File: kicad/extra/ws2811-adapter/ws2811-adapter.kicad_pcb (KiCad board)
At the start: 2 copper layers, 70 x 30 mm, 12 parts, among them J1 Conn_01x03_Pin, J2 RJ45 P1, J3 RJ45 P2, J4 RJ45 P3, J5 Conn_01x03_Socket

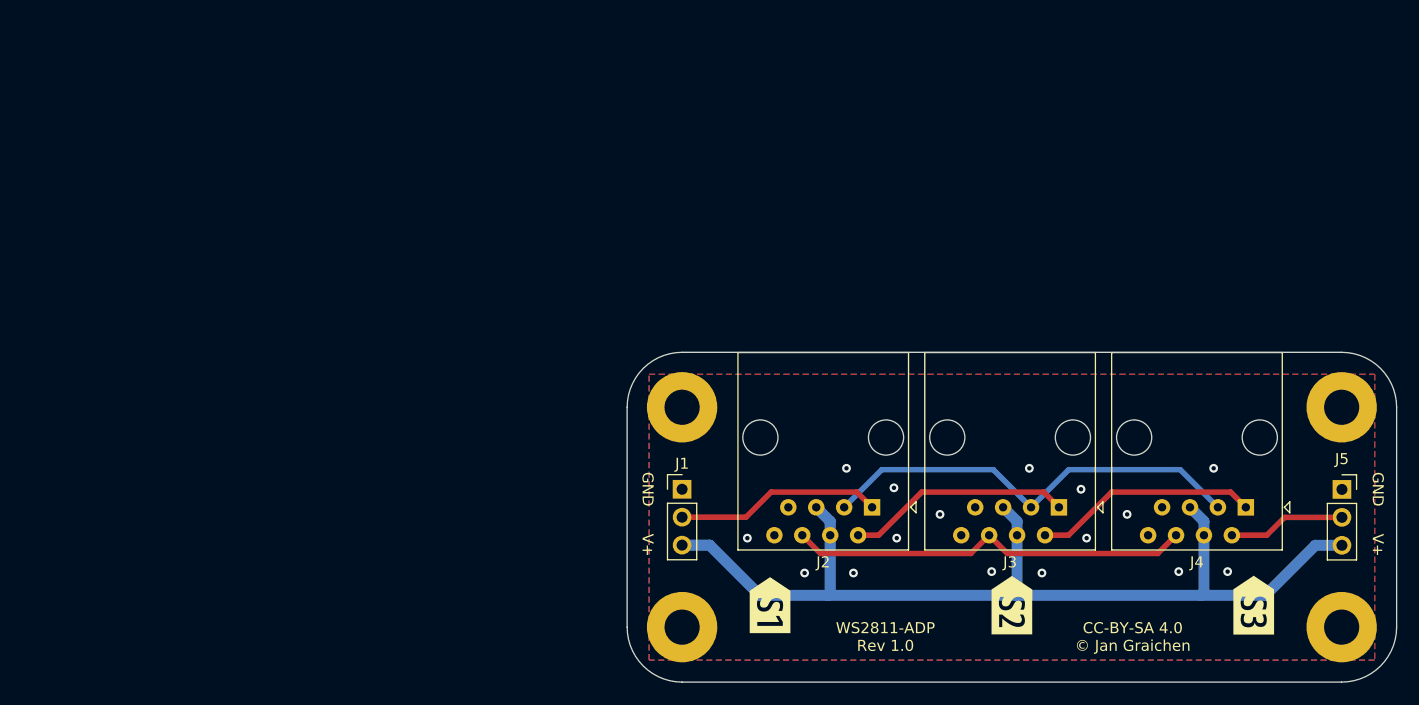
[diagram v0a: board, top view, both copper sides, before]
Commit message: feat: Rework WS2811 boards (Rev 2.0)
* Change RJ45 pinout: The data signal is always paired with a ground
  line to increase signal stability, and the changed wireing eases the
  traces on the boards.

* All WS2811 driver boards have a three pin header for direct drive now.
  They can be directly connected to a signal decoder, e.g. for testing.

* The adapter boards has jumper pins to bypass RJ45 jacks, in case you
  want to connect another board using the final pin header.

* Change pin header component to a better available JCSC parts number.

* Move RJ45 jacks on driver boards a bit more off the board, so that
  there is less space between the jack and the outer side of the Watti
  carrier. This makes it easier to plug in and out RJ45 cables as
  the latches are easier to reach.

Fixes #4
Fixes #5
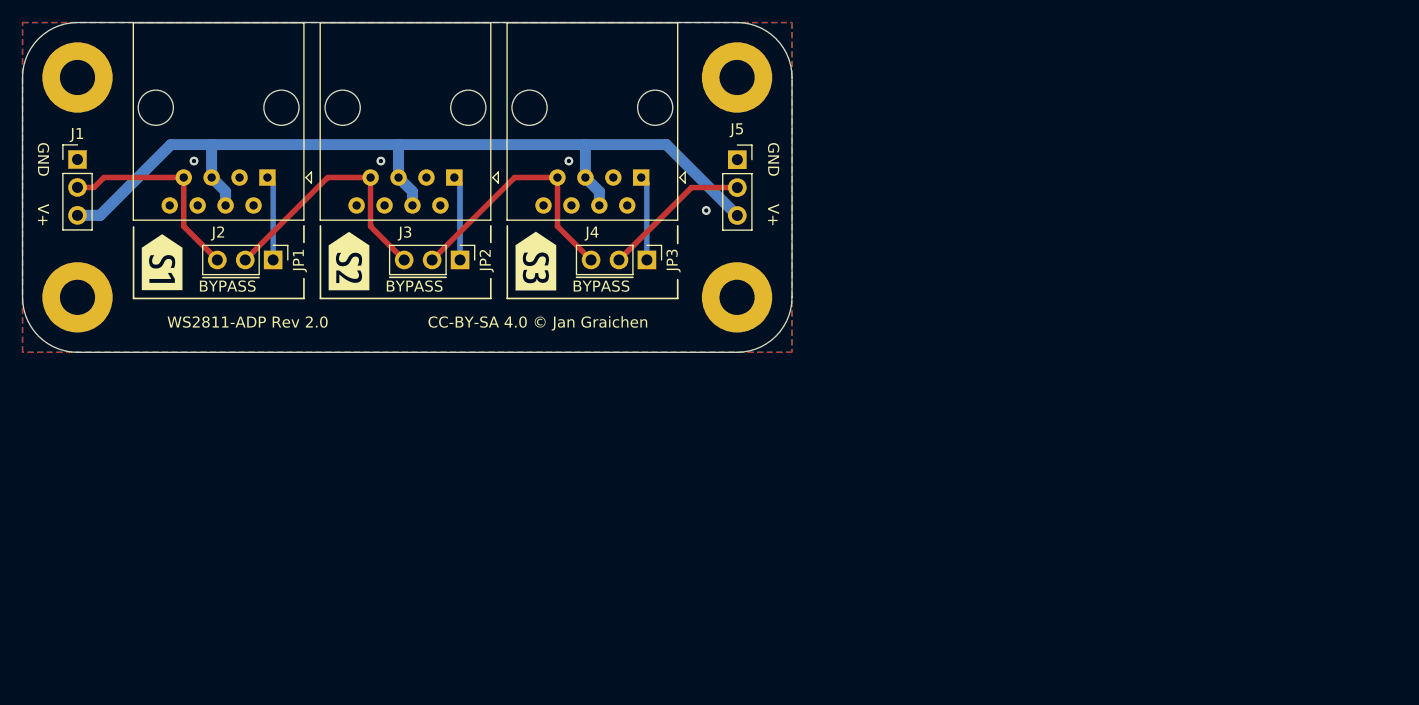
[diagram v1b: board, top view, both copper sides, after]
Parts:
- added JP1: Jumper_3_Bridged12, Connector_PinHeader_2.54mm:PinHeader_1x03_P2.54mm_Vertical, F.Cu at (87.8, 71.6)
- added JP2: Jumper_3_Bridged12, Connector_PinHeader_2.54mm:PinHeader_1x03_P2.54mm_Vertical, F.Cu at (104.8, 71.6)
- added JP3: Jumper_3_Bridged12, Connector_PinHeader_2.54mm:PinHeader_1x03_P2.54mm_Vertical, F.Cu at (121.8, 71.6)
- moved kibuzzard-6563BF6D 72.4 mm to (111.7, 71.7)
- moved kibuzzard-6563BF69 67.9 mm to (94.7, 71.7)
- moved kibuzzard-6563BF62 63.5 mm to (77.7, 71.8)
- moved J1 62.6 mm to (70.0, 62.5)
- moved J2 62.6 mm to (87.3, 64.1)
- moved J3 62.6 mm to (104.3, 64.1)
- moved J4 62.6 mm to (121.3, 64.1)
- moved J5 62.6 mm to (130.0, 62.5)
- moved REF** 62.6 mm to (70.0, 55.0)
- moved REF** 62.6 mm to (130.0, 55.0)
- moved REF** 62.6 mm to (70.0, 75.0)
- moved REF** 62.6 mm to (130.0, 75.0)
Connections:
- J2 pad 1: Net-(J1-Pin_2) -> Net-(JP1-A)
- J2 pad 2: Net-(J2-Pad2) -> GND
- J2 pad 3: Net-(J2-Pad3) -> GND
- J2 pad 6: Net-(J2-Pad6) -> GND
- J2 pad 7: GND -> Net-(J1-Pin_2)
- J3 pad 1: Net-(J2-Pad2) -> Net-(JP2-A)
- J3 pad 2: Net-(J3-Pad2) -> GND
- J3 pad 3: Net-(J2-Pad3) -> GND
- J3 pad 6: Net-(J2-Pad6) -> GND
- J3 pad 7: GND -> Net-(JP1-C)
- J4 pad 1: Net-(J3-Pad2) -> Net-(JP3-A)
- J4 pad 2: Net-(J5-Pin_2) -> GND
- J4 pad 3: Net-(J2-Pad3) -> GND
- J4 pad 6: Net-(J2-Pad6) -> GND
- J4 pad 7: GND -> Net-(JP2-C)
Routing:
- net Net-(J2-Pad3): track 39.7 -> 0.00 mm
- net Net-(J2-Pad6): track 36.7 -> 0.00 mm
- net Net-(JP2-C): track 0.00 -> 23.3 mm
- net Net-(JP1-C): track 0.00 -> 23.3 mm
- net Net-(J3-Pad2): track 20.5 -> 0.00 mm
- net Net-(J2-Pad2): track 20.5 -> 0.00 mm
- net Net-(JP3-A): track 0.00 -> 7.71 mm
- net Net-(JP2-A): track 0.00 -> 7.71 mm
- net Net-(JP1-A): track 0.00 -> 7.71 mm
- net VCC: track 89.6 -> 83.6 mm
- net Net-(J5-Pin_2): track 10.7 -> 13.5 mm
- net GND: vias 16 -> 4
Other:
- board text added: "BYPASS"
- board text added: "WS2811-ADP Rev ${REVISION}"
- board text removed: "WS2811-ADP Rev 1.0"
